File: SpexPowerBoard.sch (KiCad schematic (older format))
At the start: 10 parts

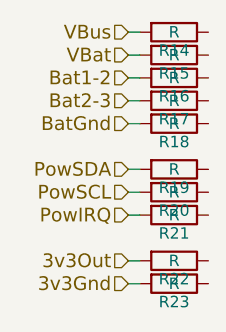
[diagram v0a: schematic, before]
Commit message: updated component numbering
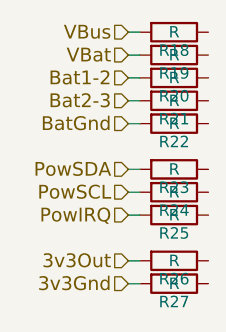
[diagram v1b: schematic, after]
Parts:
- renumbered R14 to R18, R15 to R19, R16 to R20, R17 to R21, R18 to R22, R19 to R23, R20 to R24, R21 to R25, R22 to R26, R23 to R27
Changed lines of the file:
@@
 3v3Gnd
 $Comp
-L R R14
+L R R18
 U 1 1 56DE6203
 P 2150 800
-F 0 "R14" V 2230 800 50  0000 C CNN
+F 0 "R18" V 2230 800 50  0000 C CNN
 F 1 "R" V 2150 800 50  0000 C CNN
 F 2 "" V 2080 800 50  0000 C CNN
@@
 $EndComp
 $Comp
-L R R15
+L R R19
 U 1 1 56DE621B
 P 2150 900
-F 0 "R15" V 2230 900 50  0000 C CNN
+F 0 "R19" V 2230 900 50  0000 C CNN
 F 1 "R" V 2150 900 50  0000 C CNN
 F 2 "" V 2080 900 50  0000 C CNN
@@
 $EndComp
 $Comp
-L R R16
+L R R20
 U 1 1 56DE6236
 P 2150 1000
-F 0 "R16" V 2230 1000 50  0000 C CNN
+F 0 "R20" V 2230 1000 50  0000 C CNN
 F 1 "R" V 2150 1000 50  0000 C CNN
 F 2 "" V 2080 1000 50  0000 C CNN
@@
 $EndComp
 $Comp
-L R R17
+L R R21
 U 1 1 56DE6251
 P 2150 1100
-F 0 "R17" V 2230 1100 50  0000 C CNN
+F 0 "R21" V 2230 1100 50  0000 C CNN
 F 1 "R" V 2150 1100 50  0000 C CNN
 F 2 "" V 2080 1100 50  0000 C CNN
@@
 $EndComp
 $Comp
-L R R18
+L R R22
 U 1 1 56DE626E
 P 2150 1200
-F 0 "R18" V 2230 1200 50  0000 C CNN
+F 0 "R22" V 2230 1200 50  0000 C CNN
 F 1 "R" V 2150 1200 50  0000 C CNN
 F 2 "" V 2080 1200 50  0000 C CNN
@@
 $EndComp
 $Comp
-L R R19
+L R R23
 U 1 1 56DE6291
 P 2150 1400
-F 0 "R19" V 2230 1400 50  0000 C CNN
+F 0 "R23" V 2230 1400 50  0000 C CNN
 F 1 "R" V 2150 1400 50  0000 C CNN
 F 2 "" V 2080 1400 50  0000 C CNN
@@
 $EndComp
 $Comp
-L R R20
+L R R24
 U 1 1 56DE62B4
 P 2150 1500
-F 0 "R20" V 2230 1500 50  0000 C CNN
+F 0 "R24" V 2230 1500 50  0000 C CNN
 F 1 "R" V 2150 1500 50  0000 C CNN
 F 2 "" V 2080 1500 50  0000 C CNN
@@
 $EndComp
 $Comp
-L R R21
+L R R25
 U 1 1 56DE62DB
 P 2150 1600
-F 0 "R21" V 2230 1600 50  0000 C CNN
+F 0 "R25" V 2230 1600 50  0000 C CNN
 F 1 "R" V 2150 1600 50  0000 C CNN
 F 2 "" V 2080 1600 50  0000 C CNN
@@
 $EndComp
 $Comp
-L R R22
+L R R26
 U 1 1 56DE6304
 P 2150 1800
-F 0 "R22" V 2230 1800 50  0000 C CNN
+F 0 "R26" V 2230 1800 50  0000 C CNN
 F 1 "R" V 2150 1800 50  0000 C CNN
 F 2 "" V 2080 1800 50  0000 C CNN
@@
 $EndComp
 $Comp
-L R R23
+L R R27
 U 1 1 56DE632D
 P 2150 1900
-F 0 "R23" V 2230 1900 50  0000 C CNN
+F 0 "R27" V 2230 1900 50  0000 C CNN
 F 1 "R" V 2150 1900 50  0000 C CNN
 F 2 "" V 2080 1900 50  0000 C CNN

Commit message: Schematics updated/components generated/PCB started
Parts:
- R18, R19, R20, R21, R22, R23, R24, R25, R26, R27: footprint (none) -> Resistors_SMD:R_0603
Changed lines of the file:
@@
 LIBS:parts
 LIBS:PRESSURE-BMP180_LGA7_
+LIBS:74xgxx
+LIBS:ac-dc
+LIBS:actel
+LIBS:Altera
+LIBS:analog_devices
+LIBS:brooktre
+LIBS:cmos_ieee
+LIBS:dc-dc
+LIBS:diode
+LIBS:elec-unifil
+LIBS:ESD_Protection
+LIBS:ftdi
+LIBS:gennum
+LIBS:graphic
+LIBS:hc11
+LIBS:ir
+LIBS:Lattice
+LIBS:logo
+LIBS:maxim
+LIBS:microchip_dspic33dsc
+LIBS:microchip_pic10mcu
+LIBS:microchip_pic12mcu
+LIBS:microchip_pic16mcu
+LIBS:microchip_pic18mcu
+LIBS:microchip_pic32mcu
+LIBS:motor_drivers
+LIBS:msp430
+LIBS:nordicsemi
+LIBS:nxp_armmcu
+LIBS:onsemi
+LIBS:Oscillators
+LIBS:Power_Management
+LIBS:powerint
+LIBS:pspice
+LIBS:references
+LIBS:relays
+LIBS:rfcom
+LIBS:sensors
+LIBS:silabs
+LIBS:stm8
+LIBS:stm32
+LIBS:supertex
+LIBS:switches
+LIBS:transf
+LIBS:ttl_ieee
+LIBS:video
+LIBS:Xicor
+LIBS:Zilog
 LIBS:Spex-Mainboard-Hardware-cache
 EELAYER 25 0
@@
 F 0 "R18" V 2230 800 50  0000 C CNN
 F 1 "R" V 2150 800 50  0000 C CNN
-F 2 "" V 2080 800 50  0000 C CNN
+F 2 "Resistors_SMD:R_0603" V 2080 800 50  0001 C CNN
 F 3 "" H 2150 800 50  0000 C CNN
 	1    2150 800
@@
 F 0 "R19" V 2230 900 50  0000 C CNN
 F 1 "R" V 2150 900 50  0000 C CNN
-F 2 "" V 2080 900 50  0000 C CNN
+F 2 "Resistors_SMD:R_0603" V 2080 900 50  0001 C CNN
 F 3 "" H 2150 900 50  0000 C CNN
 	1    2150 900
@@
 F 0 "R20" V 2230 1000 50  0000 C CNN
 F 1 "R" V 2150 1000 50  0000 C CNN
-F 2 "" V 2080 1000 50  0000 C CNN
+F 2 "Resistors_SMD:R_0603" V 2080 1000 50  0001 C CNN
 F 3 "" H 2150 1000 50  0000 C CNN
 	1    2150 1000
@@
 F 0 "R21" V 2230 1100 50  0000 C CNN
 F 1 "R" V 2150 1100 50  0000 C CNN
-F 2 "" V 2080 1100 50  0000 C CNN
+F 2 "Resistors_SMD:R_0603" V 2080 1100 50  0001 C CNN
 F 3 "" H 2150 1100 50  0000 C CNN
 	1    2150 1100
@@
 F 0 "R22" V 2230 1200 50  0000 C CNN
 F 1 "R" V 2150 1200 50  0000 C CNN
-F 2 "" V 2080 1200 50  0000 C CNN
+F 2 "Resistors_SMD:R_0603" V 2080 1200 50  0001 C CNN
 F 3 "" H 2150 1200 50  0000 C CNN
 	1    2150 1200
@@
 F 0 "R23" V 2230 1400 50  0000 C CNN
 F 1 "R" V 2150 1400 50  0000 C CNN
-F 2 "" V 2080 1400 50  0000 C CNN
+F 2 "Resistors_SMD:R_0603" V 2080 1400 50  0001 C CNN
 F 3 "" H 2150 1400 50  0000 C CNN
 	1    2150 1400
@@
 F 0 "R24" V 2230 1500 50  0000 C CNN
 F 1 "R" V 2150 1500 50  0000 C CNN
-F 2 "" V 2080 1500 50  0000 C CNN
+F 2 "Resistors_SMD:R_0603" V 2080 1500 50  0001 C CNN
 F 3 "" H 2150 1500 50  0000 C CNN
 	1    2150 1500
@@
 F 0 "R25" V 2230 1600 50  0000 C CNN
 F 1 "R" V 2150 1600 50  0000 C CNN
-F 2 "" V 2080 1600 50  0000 C CNN
+F 2 "Resistors_SMD:R_0603" V 2080 1600 50  0001 C CNN
 F 3 "" H 2150 1600 50  0000 C CNN
 	1    2150 1600
@@
 F 0 "R26" V 2230 1800 50  0000 C CNN
 F 1 "R" V 2150 1800 50  0000 C CNN
-F 2 "" V 2080 1800 50  0000 C CNN
+F 2 "Resistors_SMD:R_0603" V 2080 1800 50  0001 C CNN
 F 3 "" H 2150 1800 50  0000 C CNN
 	1    2150 1800
@@
 F 0 "R27" V 2230 1900 50  0000 C CNN
 F 1 "R" V 2150 1900 50  0000 C CNN
-F 2 "" V 2080 1900 50  0000 C CNN
+F 2 "Resistors_SMD:R_0603" V 2080 1900 50  0001 C CNN
 F 3 "" H 2150 1900 50  0000 C CNN
 	1    2150 1900

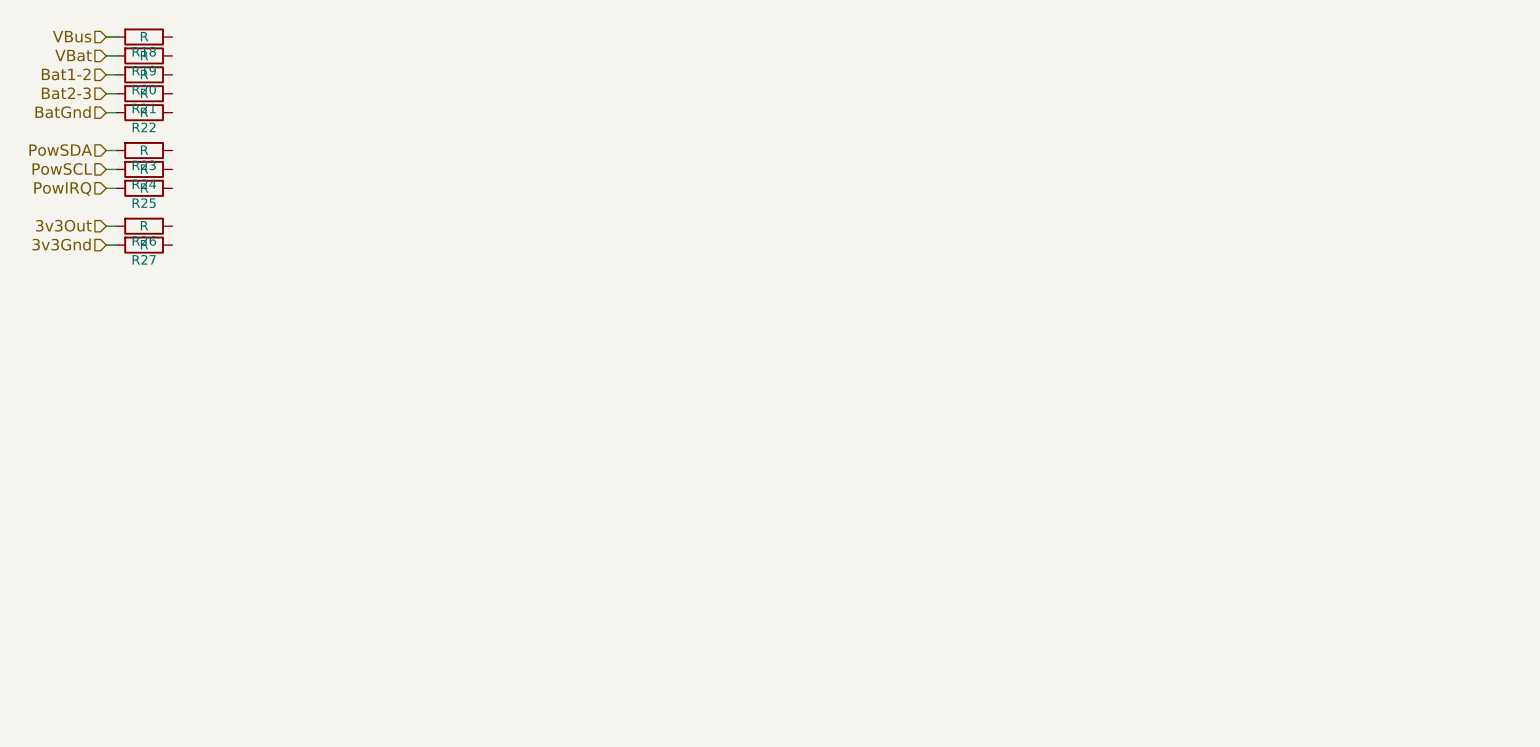
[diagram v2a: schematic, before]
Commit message: Added power board to both sch and pcb. Will route when ready for it
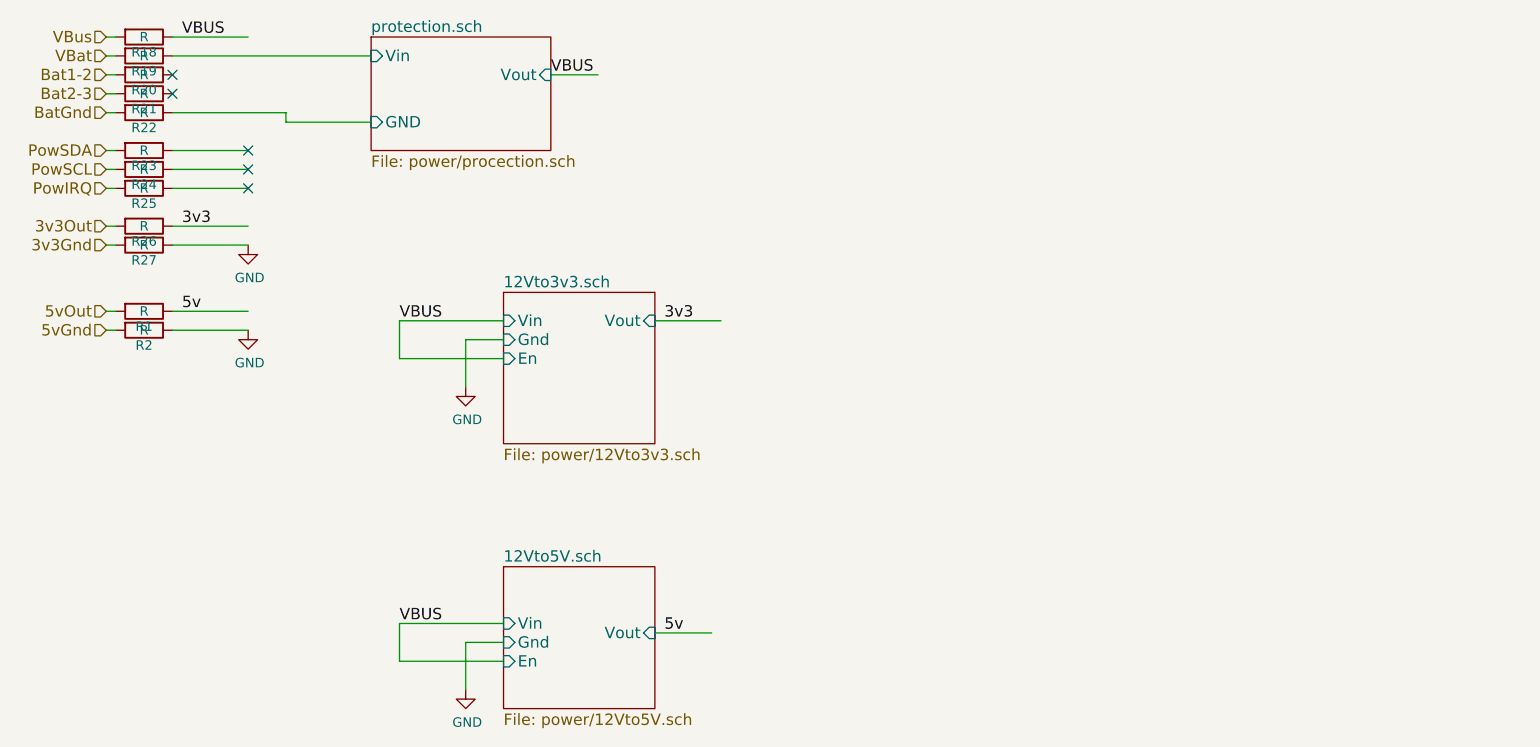
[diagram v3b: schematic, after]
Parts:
- added R1, R2: R, Resistors_SMD:R_0603, symbol R
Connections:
- net labels added: 3v3, 5v, 5vGnd, 5vOut, GND, VBUS
- wire segments 10 -> 37
- no-connect marks 0 -> 5

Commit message: working on PCB layout
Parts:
- renumbered R1 to R39, R2 to R40
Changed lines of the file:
@@
 LIBS:contrib
 LIBS:valves
+LIBS:parts
+LIBS:PRESSURE-BMP180_LGA7_
+LIBS:74xgxx
+LIBS:ac-dc
+LIBS:actel
+LIBS:Altera
+LIBS:analog_devices
+LIBS:brooktre
+LIBS:cmos_ieee
+LIBS:dc-dc
+LIBS:diode
+LIBS:elec-unifil
+LIBS:ESD_Protection
+LIBS:ftdi
+LIBS:gennum
+LIBS:graphic
+LIBS:hc11
+LIBS:ir
+LIBS:Lattice
+LIBS:logo
+LIBS:maxim
+LIBS:microchip_dspic33dsc
+LIBS:microchip_pic10mcu
+LIBS:microchip_pic12mcu
+LIBS:microchip_pic16mcu
+LIBS:microchip_pic18mcu
+LIBS:microchip_pic32mcu
+LIBS:motor_drivers
+LIBS:msp430
+LIBS:nordicsemi
+LIBS:nxp_armmcu
+LIBS:onsemi
+LIBS:Oscillators
+LIBS:Power_Management
+LIBS:powerint
+LIBS:pspice
+LIBS:references
+LIBS:relays
+LIBS:rfcom
+LIBS:sensors
+LIBS:silabs
+LIBS:stm8
+LIBS:stm32
+LIBS:supertex
+LIBS:switches
+LIBS:transf
+LIBS:ttl_ieee
+LIBS:video
+LIBS:Xicor
+LIBS:Zilog
 LIBS:KL03-QFN24
 LIBS:lt3652
@@
 LIBS:si3407dv
 LIBS:tps563200
-LIBS:diode
-LIBS:SpexPowerBoard-cache
+LIBS:Spex-Mainboard-Hardware-cache
 EELAYER 25 0
 EELAYER END
 $Descr A4 11693 8268
 encoding utf-8
-Sheet 1 4
+Sheet 3 7
 Title ""
 Date ""
@@
 $EndComp
 $Sheet
-S 4050 2150 800  800
+S 5700 800  800  800
 U 56FE3A4E
 F0 "12Vto3v3.sch" 60
 F1 "power/12Vto3v3.sch" 60
-F2 "Vin" I L 4050 2300 60
-F3 "Gnd" I L 4050 2400 60
-F4 "En" I L 4050 2500 60
-F5 "Vout" I R 4850 2300 60
+F2 "Vin" I L 5700 950 60
+F3 "Gnd" I L 5700 1050 60
+F4 "En" I L 5700 1150 60
+F5 "Vout" I R 6500 950 60
 $EndSheet
 $Sheet
@@
 Text Label 4300 1000 0    60   ~ 0
 VBUS
-Text Label 3500 2300 0    60   ~ 0
+Text Label 5150 950  0    60   ~ 0
 VBUS
 $Comp
-L GND #PWR3
+L GND #PWR056
 U 1 1 56FE58A8
-P 3850 2650
-F 0 "#PWR3" H 3850 2400 50  0001 C CNN
-F 1 "GND" H 3858 2477 50  0000 C CNN
-F 2 "" H 3850 2650 50  0000 C CNN
-F 3 "" H 3850 2650 50  0000 C CNN
-	1    3850 2650
+P 5500 1300
+F 0 "#PWR056" H 5500 1050 50  0001 C CNN
+F 1 "GND" H 5508 1127 50  0000 C CNN
+F 2 "" H 5500 1300 50  0000 C CNN
+F 3 "" H 5500 1300 50  0000 C CNN
+	1    5500 1300
 	1    0    0    -1
 $EndComp
@@
 	4300 1000 4550 1000
 Wire Wire Line
-	4050 2300 3500 2300
-Wire Wire Line
-	4050 2500 3500 2500
-Wire Wire Line
-	3500 2500 3500 2300
-Wire Wire Line
-	3850 2400 4050 2400
-Wire Wire Line
-	3850 2400 3850 2650
-Wire Wire Line
-	4850 2300 5200 2300
-Text Label 4900 2300 0    60   ~ 0
+	5700 950  5150 950
+Wire Wire Line
+	5700 1150 5150 1150
+Wire Wire Line
+	5150 1150 5150 950
+Wire Wire Line
+	5500 1050 5700 1050
+Wire Wire Line
+	5500 1050 5500 1300
+Wire Wire Line
+	6500 950  6850 950
+Text Label 6550 950  0    60   ~ 0
 3v3
-Text Label 3500 3900 0    60   ~ 0
+Text Label 7550 1100 0    60   ~ 0
 VBUS
 $Comp
-L GND #PWR4
+L GND #PWR057
 U 1 1 56FE6215
-P 3850 4250
-F 0 "#PWR4" H 3850 4000 50  0001 C CNN
-F 1 "GND" H 3858 4077 50  0000 C CNN
-F 2 "" H 3850 4250 50  0000 C CNN
-F 3 "" H 3850 4250 50  0000 C CNN
-	1    3850 4250
+P 7900 1450
+F 0 "#PWR057" H 7900 1200 50  0001 C CNN
+F 1 "GND" H 7908 1277 50  0000 C CNN
+F 2 "" H 7900 1450 50  0000 C CNN
+F 3 "" H 7900 1450 50  0000 C CNN
+	1    7900 1450
 	1    0    0    -1
 $EndComp
 Wire Wire Line
-	4050 3900 3500 3900
-Wire Wire Line
-	4050 4100 3500 4100
-Wire Wire Line
-	3500 4100 3500 3900
-Wire Wire Line
-	3850 4000 4050 4000
-Wire Wire Line
-	3850 4000 3850 4250
+	8100 1100 7550 1100
+Wire Wire Line
+	8100 1300 7550 1300
+Wire Wire Line
+	7550 1300 7550 1100
+Wire Wire Line
+	7900 1200 8100 1200
+Wire Wire Line
+	7900 1200 7900 1450
 $Sheet
-S 4050 3600 800  750
+S 8100 800  800  750
 U 56FE62EA
 F0 "12Vto5V.sch" 60
 F1 "power/12Vto5V.sch" 60
-F2 "Vin" I L 4050 3900 60
-F3 "Gnd" I L 4050 4000 60
-F4 "En" I L 4050 4100 60
-F5 "Vout" I R 4850 3950 60
+F2 "Vin" I L 8100 1100 60
+F3 "Gnd" I L 8100 1200 60
+F4 "En" I L 8100 1300 60
+F5 "Vout" I R 8900 1150 60
 $EndSheet
 Wire Wire Line
-	4850 3950 5150 3950
-Text Label 4900 3950 0    60   ~ 0
+	8900 1150 9200 1150
+Text Label 8950 1150 0    60   ~ 0
 5v
 Wire Wire Line
@@
 3v3
 $Comp
-L GND #PWR1
+L GND #PWR058
 U 1 1 56FE74FE
 P 2700 1900
-F 0 "#PWR1" H 2700 1650 50  0001 C CNN
+F 0 "#PWR058" H 2700 1650 50  0001 C CNN
 F 1 "GND" H 2708 1727 50  0000 C CNN
 F 2 "" H 2700 1900 50  0000 C CNN
@@
 5vGnd
 $Comp
-L R R1
+L R R39
 U 1 1 56FE7B52
 P 2150 2250
-F 0 "R1" V 2230 2250 50  0000 C CNN
+F 0 "R39" V 2230 2250 50  0000 C CNN
 F 1 "R" V 2150 2250 50  0000 C CNN
 F 2 "Resistors_SMD:R_0603" V 2080 2250 50  0001 C CNN
@@
 $EndComp
 $Comp
-L R R2
+L R R40
 U 1 1 56FE7B58
 P 2150 2350
-F 0 "R2" V 2230 2350 50  0000 C CNN
+F 0 "R40" V 2230 2350 50  0000 C CNN
 F 1 "R" V 2150 2350 50  0000 C CNN
 F 2 "Resistors_SMD:R_0603" V 2080 2350 50  0001 C CNN
@@
 5v
 $Comp
-L GND #PWR2
+L GND #PWR059
 U 1 1 56FE7B63
 P 2700 2350
-F 0 "#PWR2" H 2700 2100 50  0001 C CNN
+F 0 "#PWR059" H 2700 2100 50  0001 C CNN
 F 1 "GND" H 2708 2177 50  0000 C CNN
 F 2 "" H 2700 2350 50  0000 C CNN

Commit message: schematic updated
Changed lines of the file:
@@
 LIBS:valves
 LIBS:parts
-LIBS:PRESSURE-BMP180_LGA7_
 LIBS:74xgxx
 LIBS:ac-dc
@@
 $EndComp
 $Sheet
-S 5700 800  800  800
+S 4050 2150 800  800
 U 56FE3A4E
 F0 "12Vto3v3.sch" 60
 F1 "power/12Vto3v3.sch" 60
-F2 "Vin" I L 5700 950 60
-F3 "Gnd" I L 5700 1050 60
-F4 "En" I L 5700 1150 60
-F5 "Vout" I R 6500 950 60
+F2 "Vin" I L 4050 2300 60
+F3 "Gnd" I L 4050 2400 60
+F4 "En" I L 4050 2500 60
+F5 "Vout" I R 4850 2300 60
 $EndSheet
 $Sheet
@@
 Text Label 4300 1000 0    60   ~ 0
 VBUS
-Text Label 5150 950  0    60   ~ 0
+Text Label 3500 2300 0    60   ~ 0
 VBUS
 $Comp
-L GND #PWR056
+L GND #PWR058
 U 1 1 56FE58A8
-P 5500 1300
-F 0 "#PWR056" H 5500 1050 50  0001 C CNN
-F 1 "GND" H 5508 1127 50  0000 C CNN
-F 2 "" H 5500 1300 50  0000 C CNN
-F 3 "" H 5500 1300 50  0000 C CNN
-	1    5500 1300
+P 3850 2650
+F 0 "#PWR058" H 3850 2400 50  0001 C CNN
+F 1 "GND" H 3858 2477 50  0000 C CNN
+F 2 "" H 3850 2650 50  0000 C CNN
+F 3 "" H 3850 2650 50  0000 C CNN
+	1    3850 2650
 	1    0    0    -1
 $EndComp
@@
 	4300 1000 4550 1000
 Wire Wire Line
-	5700 950  5150 950
-Wire Wire Line
-	5700 1150 5150 1150
-Wire Wire Line
-	5150 1150 5150 950
-Wire Wire Line
-	5500 1050 5700 1050
-Wire Wire Line
-	5500 1050 5500 1300
-Wire Wire Line
-	6500 950  6850 950
-Text Label 6550 950  0    60   ~ 0
+	4050 2300 3500 2300
+Wire Wire Line
+	4050 2500 3500 2500
+Wire Wire Line
+	3500 2500 3500 2300
+Wire Wire Line
+	3850 2400 4050 2400
+Wire Wire Line
+	3850 2400 3850 2650
+Wire Wire Line
+	4850 2300 5200 2300
+Text Label 4900 2300 0    60   ~ 0
 3v3
-Text Label 7550 1100 0    60   ~ 0
+Text Label 3500 3900 0    60   ~ 0
 VBUS
 $Comp
-L GND #PWR057
+L GND #PWR059
 U 1 1 56FE6215
-P 7900 1450
-F 0 "#PWR057" H 7900 1200 50  0001 C CNN
-F 1 "GND" H 7908 1277 50  0000 C CNN
-F 2 "" H 7900 1450 50  0000 C CNN
-F 3 "" H 7900 1450 50  0000 C CNN
-	1    7900 1450
+P 3850 4250
+F 0 "#PWR059" H 3850 4000 50  0001 C CNN
+F 1 "GND" H 3858 4077 50  0000 C CNN
+F 2 "" H 3850 4250 50  0000 C CNN
+F 3 "" H 3850 4250 50  0000 C CNN
+	1    3850 4250
 	1    0    0    -1
 $EndComp
 Wire Wire Line
-	8100 1100 7550 1100
-Wire Wire Line
-	8100 1300 7550 1300
-Wire Wire Line
-	7550 1300 7550 1100
-Wire Wire Line
-	7900 1200 8100 1200
-Wire Wire Line
-	7900 1200 7900 1450
+	4050 3900 3500 3900
+Wire Wire Line
+	4050 4100 3500 4100
+Wire Wire Line
+	3500 4100 3500 3900
+Wire Wire Line
+	3850 4000 4050 4000
+Wire Wire Line
+	3850 4000 3850 4250
 $Sheet
-S 8100 800  800  750
+S 4050 3600 800  750
 U 56FE62EA
 F0 "12Vto5V.sch" 60
 F1 "power/12Vto5V.sch" 60
-F2 "Vin" I L 8100 1100 60
-F3 "Gnd" I L 8100 1200 60
-F4 "En" I L 8100 1300 60
-F5 "Vout" I R 8900 1150 60
+F2 "Vin" I L 4050 3900 60
+F3 "Gnd" I L 4050 4000 60
+F4 "En" I L 4050 4100 60
+F5 "Vout" I R 4850 3950 60
 $EndSheet
 Wire Wire Line
-	8900 1150 9200 1150
-Text Label 8950 1150 0    60   ~ 0
+	4850 3950 5150 3950
+Text Label 4900 3950 0    60   ~ 0
 5v
 Wire Wire Line
@@
 3v3
 $Comp
-L GND #PWR058
+L GND #PWR060
 U 1 1 56FE74FE
 P 2700 1900
-F 0 "#PWR058" H 2700 1650 50  0001 C CNN
+F 0 "#PWR060" H 2700 1650 50  0001 C CNN
 F 1 "GND" H 2708 1727 50  0000 C CNN
 F 2 "" H 2700 1900 50  0000 C CNN
@@
 5v
 $Comp
-L GND #PWR059
+L GND #PWR061
 U 1 1 56FE7B63
 P 2700 2350
-F 0 "#PWR059" H 2700 2100 50  0001 C CNN
+F 0 "#PWR061" H 2700 2100 50  0001 C CNN
 F 1 "GND" H 2708 2177 50  0000 C CNN
 F 2 "" H 2700 2350 50  0000 C CNN
